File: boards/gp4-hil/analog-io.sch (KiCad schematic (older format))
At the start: 155 parts, among them U10 AD9609, U11 DAC084S085, U12 DAC084S085, U13 DAC084S085, U14 DAC084S085, U19 TS3A4751, U2 XC7A100T-1FTG256C, U25 TS3A4751, U26 TS3A4751, U27 TS3A4751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

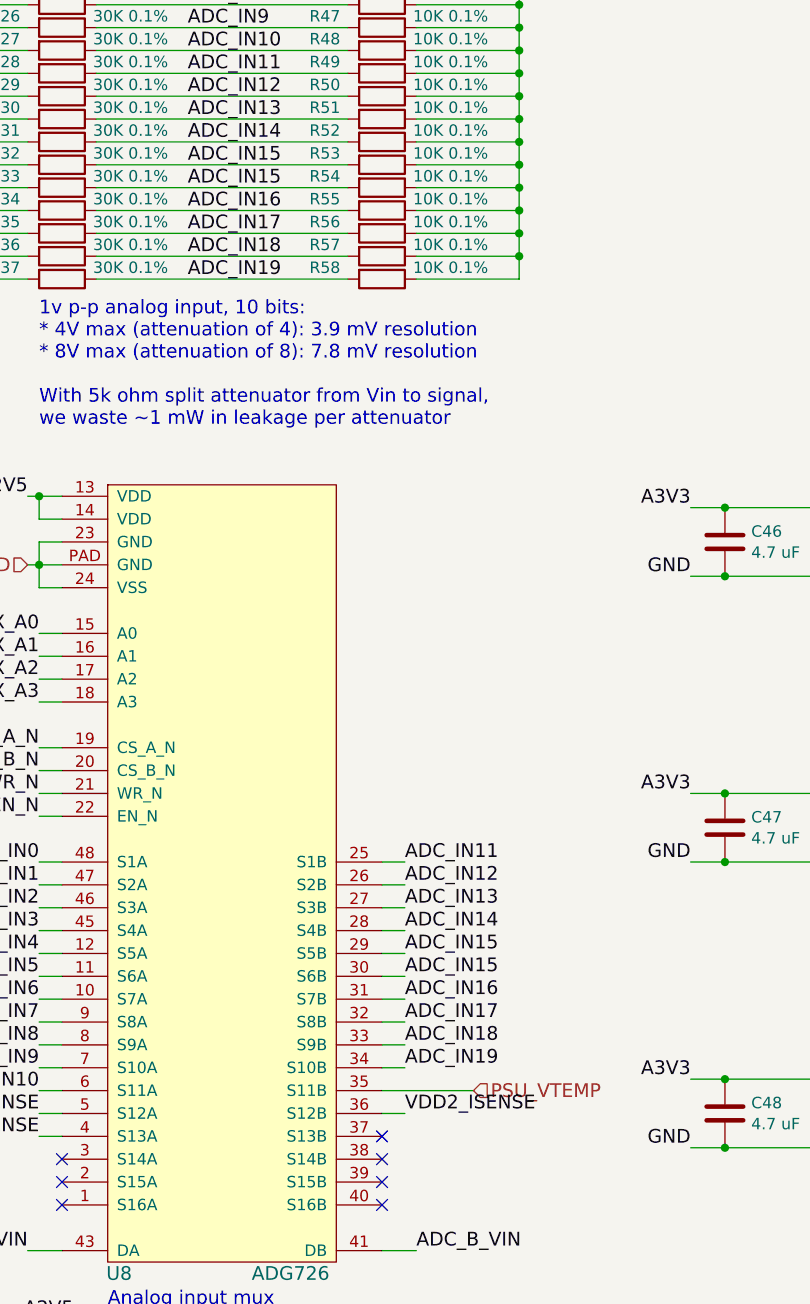
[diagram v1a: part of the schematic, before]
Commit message: Began work on analog mux input routing. Needs more work.
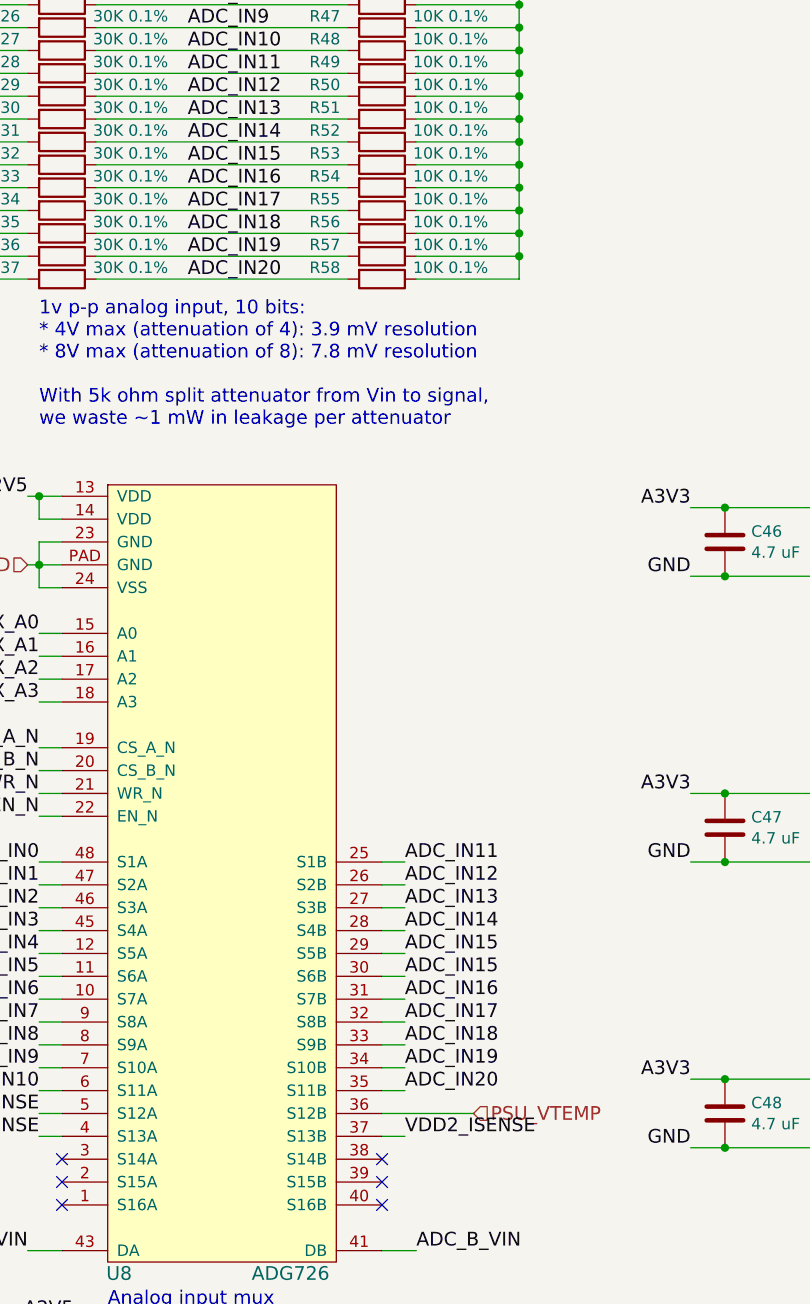
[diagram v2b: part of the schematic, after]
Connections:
- net ADC_IN15: no longer R33.1, R54.2
- net ADC_IN16: now also R33.1, R54.2; no longer R34.1, R55.2
- net ADC_IN17: now also R34.1, R55.2; no longer R35.1, R56.2
- net ADC_IN18: now also R35.1, R56.2; no longer R36.1, R57.2
- net ADC_IN19: now also R36.1, R57.2; no longer R37.1, R58.2
- net PSU_VTEMP: now also U8.36 (S12B); no longer U8.35 (S11B)
- net VDD2_ISENSE: now also U8.37 (S13B); no longer U8.36 (S12B)
- new net ADC_IN20: R37.1, R58.2, U8.35 (S11B)
- no-connect marks 14 -> 13
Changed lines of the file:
@@
 ADC_IN15
 Text Label 2200 2300 0    60   ~ 0
-ADC_IN15
-Text Label 2200 2400 0    60   ~ 0
 ADC_IN16
-Text Label 2200 2500 0    60   ~ 0
+Text Label 2200 2400 0    60   ~ 0
 ADC_IN17
-Text Label 2200 2600 0    60   ~ 0
+Text Label 2200 2500 0    60   ~ 0
 ADC_IN18
+Text Label 2200 2600 0    60   ~ 0
+ADC_IN19
 Text Label 1500 3650 2    60   ~ 0
 A2V5
@@
 NoConn ~ 1650 6650
 NoConn ~ 1650 6750
-NoConn ~ 3050 6450
 NoConn ~ 3050 6550
 NoConn ~ 3050 6650
@@
 	3050 6050 3150 6050
 Wire Wire Line
-	3050 6250 3450 6250
+	3050 6350 3450 6350
 Wire Wire Line
 	1700 7550 2950 7550
@@
 NoConn ~ 7650 7800
 NoConn ~ 7650 7600
-Text HLabel 3450 6250 2    60   Input ~ 0
+Text HLabel 3450 6350 2    60   Input ~ 0
 PSU_VTEMP
 Wire Wire Line
@@
 DUT_VDD2
 Text Label 2200 2700 0    60   ~ 0
-ADC_IN19
+ADC_IN20
 Wire Wire Line
 	1800 2700 2900 2700
@@
 Text Label 1550 6450 2    60   ~ 0
 VDD1_ISENSE
-Text Label 3150 6350 0    60   ~ 0
+Text Label 3150 6450 0    60   ~ 0
 VDD2_ISENSE
 Wire Wire Line
-	3150 6350 3050 6350
+	3150 6450 3050 6450
 Wire Wire Line
 	1650 6450 1550 6450
@@
 NoConn ~ 20650 5650
 NoConn ~ 20650 5750
+Text Label 3150 6250 0    60   ~ 0
+ADC_IN20
+Wire Wire Line
+	3150 6250 3050 6250
 $EndSCHEMATC

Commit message: Saving current layout before tweaking attenuators
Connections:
- net ADC_IN0: now also U8.32 (S8B); no longer U8.48 (S1A)
- net ADC_IN1: now also U8.30 (S6B); no longer U8.47 (S2A)
- net ADC_IN11: now also U8.2 (S15A); no longer U8.25 (S1B)
- net ADC_IN12: now also U8.3 (S14A); no longer U8.26 (S2B)
- net ADC_IN13: now also U8.7 (S10A); no longer U8.27 (S3B)
- net ADC_IN14: now also U8.4 (S13A); no longer U8.28 (S4B)
- net ADC_IN15: now also U8.8 (S9A); no longer U8.29 (S5B), U8.30 (S6B)
- net ADC_IN16: now also U8.9 (S8A); no longer U8.31 (S7B)
- net ADC_IN17: now also U8.10 (S7A); no longer U8.32 (S8B)
- net ADC_IN18: now also U8.11 (S6A); no longer U8.33 (S9B)
- net ADC_IN19: now also U8.12 (S5A); no longer U8.34 (S10B)
- net ADC_IN2: now also U8.31 (S7B); no longer U8.46 (S3A)
- net ADC_IN20: now also U8.26 (S2B); no longer U8.35 (S11B)
- net ADC_IN3: now also U8.29 (S5B); no longer U8.45 (S4A)
- net ADC_IN4: now also U8.45 (S4A); no longer U8.12 (S5A)
- net ADC_IN5: now also U8.46 (S3A); no longer U8.11 (S6A)
- net ADC_IN6: now also U8.47 (S2A); no longer U8.10 (S7A)
- net ADC_IN7: now also U8.48 (S1A); no longer U8.9 (S8A)
- net ADC_IN8: now also U8.1 (S16A); no longer U8.8 (S9A)
- net ADC_IN9: now also U8.5 (S12A); no longer U8.7 (S10A)
- net PSU_VTEMP: now also U8.33 (S9B); no longer U8.36 (S12B)
- net VDD1_ISENSE: now also U8.28 (S4B); no longer U8.4 (S13A)
- net VDD2_ISENSE: now also U8.25 (S1B); no longer U8.37 (S13B)
- net VPP_ISENSE: now also U8.27 (S3B); no longer U8.5 (S12A)
- no-connect marks 13 -> 14
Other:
- note added: "FIXME: RC time constant with 100K ohm input impedance\nis WAAY too big. Need to cut this down by a LOT."
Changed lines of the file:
@@
 Sheet 5 7
 Title "GreenPak Hardware-In-Loop Test Platform"
-Date "2016-05-29"
+Date "2016-06-01"
 Rev "0.1"
 Comp "Andrew Zonenberg"
@@
 Text Label 1550 5050 2    60   ~ 0
 MUX_EN_N
-Text Label 1550 5250 2    60   ~ 0
+Text Label 3150 5950 0    60   ~ 0
 ADC_IN0
-Text Label 1550 5350 2    60   ~ 0
+Text Label 3150 5750 0    60   ~ 0
 ADC_IN1
-Text Label 1550 5450 2    60   ~ 0
+Text Label 3150 5850 0    60   ~ 0
 ADC_IN2
-Text Label 1550 5550 2    60   ~ 0
+Text Label 3150 5650 0    60   ~ 0
 ADC_IN3
-Text Label 1550 5650 2    60   ~ 0
+Text Label 1550 5550 2    60   ~ 0
 ADC_IN4
-Text Label 1550 5750 2    60   ~ 0
+Text Label 1550 5450 2    60   ~ 0
 ADC_IN5
-Text Label 1550 5850 2    60   ~ 0
+Text Label 1550 5350 2    60   ~ 0
 ADC_IN6
-Text Label 1550 5950 2    60   ~ 0
+Text Label 1550 5250 2    60   ~ 0
 ADC_IN7
-Text Label 1550 6050 2    60   ~ 0
+Text Label 1550 6750 2    60   ~ 0
 ADC_IN8
-Text Label 1550 6150 2    60   ~ 0
+Text Label 1550 6350 2    60   ~ 0
 ADC_IN9
 Text Label 1550 6250 2    60   ~ 0
 ADC_IN10
-Text Label 3150 5250 0    60   ~ 0
+Text Label 1550 6650 2    60   ~ 0
 ADC_IN11
-Text Label 3150 5350 0    60   ~ 0
+Text Label 1550 6550 2    60   ~ 0
 ADC_IN12
-Text Label 3150 5450 0    60   ~ 0
+Text Label 1550 6150 2    60   ~ 0
 ADC_IN13
-Text Label 3150 5550 0    60   ~ 0
+Text Label 1550 6450 2    60   ~ 0
 ADC_IN14
-Text Label 3150 5650 0    60   ~ 0
-ADC_IN15
-Text Label 3150 5750 0    60   ~ 0
+Text Label 1550 6050 2    60   ~ 0
 ADC_IN15
-Text Label 3150 5850 0    60   ~ 0
+Text Label 1550 5950 2    60   ~ 0
 ADC_IN16
-Text Label 3150 5950 0    60   ~ 0
+Text Label 1550 5850 2    60   ~ 0
 ADC_IN17
-Text Label 3150 6050 0    60   ~ 0
+Text Label 1550 5750 2    60   ~ 0
 ADC_IN18
 $Comp
@@
 	1    0    0    -1
 $EndComp
-NoConn ~ 1650 6550
-NoConn ~ 1650 6650
-NoConn ~ 1650 6750
 NoConn ~ 3050 6550
 NoConn ~ 3050 6650
@@
 	1650 5950 1550 5950
 Wire Wire Line
-	1650 6050 1550 6050
+	1650 6750 1550 6750
 Wire Wire Line
 	1550 6150 1650 6150
@@
 	1650 6250 1550 6250
 Wire Wire Line
-	3050 5250 3150 5250
-Wire Wire Line
-	3150 5350 3050 5350
-Wire Wire Line
 	3050 5450 3150 5450
 Wire Wire Line
@@
 	3050 5850 3150 5850
 Wire Wire Line
-	3150 5950 3050 5950
-Wire Wire Line
-	3050 6050 3150 6050
-Wire Wire Line
-	3050 6350 3450 6350
+	3050 6050 3450 6050
 Wire Wire Line
 	1700 7550 2950 7550
@@
 NoConn ~ 7650 7800
 NoConn ~ 7650 7600
-Text HLabel 3450 6350 2    60   Input ~ 0
+Text HLabel 3450 6050 2    60   Input ~ 0
 PSU_VTEMP
 Wire Wire Line
@@
 $EndComp
 Connection ~ 3650 2600
-Text Label 3150 6150 0    60   ~ 0
+Text Label 1550 5650 2    60   ~ 0
 ADC_IN19
 Wire Wire Line
-	3150 6150 3050 6150
+	3150 5950 3050 5950
 Wire Wire Line
 	1300 700  1500 700
@@
 Wire Wire Line
 	19000 11750 18800 11750
-Text Label 1550 6350 2    60   ~ 0
+Text Label 3150 5450 0    60   ~ 0
 VPP_ISENSE
-Text Label 1550 6450 2    60   ~ 0
+Text Label 3150 5550 0    60   ~ 0
 VDD1_ISENSE
-Text Label 3150 6450 0    60   ~ 0
+Text Label 3150 5250 0    60   ~ 0
 VDD2_ISENSE
 Wire Wire Line
-	3150 6450 3050 6450
+	3150 5250 3050 5250
 Wire Wire Line
 	1650 6450 1550 6450
@@
 NoConn ~ 20650 5650
 NoConn ~ 20650 5750
-Text Label 3150 6250 0    60   ~ 0
+Text Label 3150 5350 0    60   ~ 0
 ADC_IN20
 Wire Wire Line
-	3150 6250 3050 6250
+	3150 5350 3050 5350
+Wire Wire Line
+	1650 6650 1550 6650
+Wire Wire Line
+	1650 6550 1550 6550
+Wire Wire Line
+	1550 6050 1650 6050
+Text Notes 9850 11550 0    60   ~ 0
+FIXME: RC time constant with 100K ohm input impedance\nis WAAY too big. Need to cut this down by a LOT.
+NoConn ~ 3050 6150
+NoConn ~ 3050 6250
+NoConn ~ 3050 6350
+NoConn ~ 3050 6450
 $EndSCHEMATC
